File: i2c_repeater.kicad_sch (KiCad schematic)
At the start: 14 parts, among them J26 Conn_02x05_Odd_Even, J27 Conn_02x05_Odd_Even, U12 PCA9617ADPJ

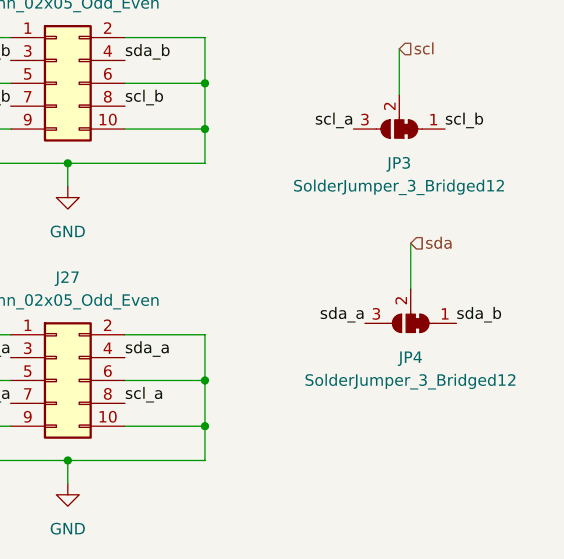
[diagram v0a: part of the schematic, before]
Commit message: silkscreen & pad changes
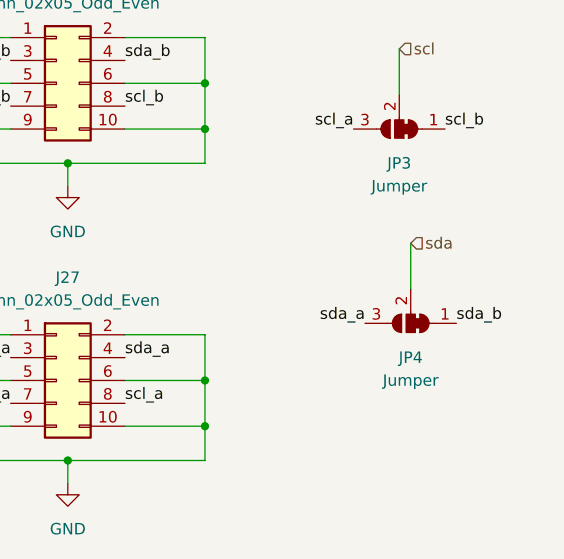
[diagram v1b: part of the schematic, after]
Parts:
- JP3, JP4: value SolderJumper_3_Bridged12 -> Jumper
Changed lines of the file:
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@@
     (in_bom yes) (on_board yes) (fields_autoplaced)
     (property "Reference" "JP4" (id 0) (at 168.91 71.12 0))
-    (property "Value" "SolderJumper_3_Bridged12" (id 1) (at 168.91 73.66 0))
+    (property "Value" "Jumper" (id 1) (at 168.91 73.66 0))
     (property "Footprint" "Jumper:SolderJumper-3_P1.3mm_Bridged12_RoundedPad1.0x1.5mm" (id 2) (at 168.91 67.31 0)
       (effects (font (size 1.27 1.27)) hide)
@@
     (in_bom yes) (on_board yes) (fields_autoplaced)
     (property "Reference" "JP3" (id 0) (at 167.64 49.53 0))
-    (property "Value" "SolderJumper_3_Bridged12" (id 1) (at 167.64 52.07 0))
+    (property "Value" "Jumper" (id 1) (at 167.64 52.07 0))
     (property "Footprint" "Jumper:SolderJumper-3_P1.3mm_Bridged12_RoundedPad1.0x1.5mm" (id 2) (at 167.64 45.72 0)
       (effects (font (size 1.27 1.27)) hide)
